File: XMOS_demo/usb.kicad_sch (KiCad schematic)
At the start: 15 parts, among them J2 Screw_Terminal, J3 Conn_01x02_Pin, J4 USB_C_Receptacle_USB2.0_16P, U3 TPD3S014

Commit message: Summary (required)
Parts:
- renumbered C22 to C30, C23 to C31, R16 to R21, R17 to R22, R24 to R23, R26 to R24, R18 to R25, R19 to R26
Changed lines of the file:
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@@
 		(on_board yes)
 		(dnp no)
-		(property "Reference" "#PWR094"
+		(property "Reference" "#PWR041"
 			(at 261.62 97.79 0)
 			(effects
@@
 			(project "XMOS_demo"
 				(path "/0a855fb0-ca19-4770-811e-70d8770d7fdd/0ad88a15-386f-4052-8899-c737373d7f63"
-					(reference "#PWR094")
+					(reference "#PWR041")
 					(unit 1)
 				)
@@
 		(on_board yes)
 		(dnp no)
-		(property "Reference" "R16"
+		(property "Reference" "R21"
 			(at 112.522 52.324 0)
 			(effects
@@
 			(project "XMOS_demo"
 				(path "/0a855fb0-ca19-4770-811e-70d8770d7fdd/0ad88a15-386f-4052-8899-c737373d7f63"
-					(reference "R16")
+					(reference "R21")
 					(unit 1)
 				)
@@
 		(on_board yes)
 		(dnp no)
-		(property "Reference" "R18"
+		(property "Reference" "R25"
 			(at 124.46 77.216 90)
 			(effects
@@
 			(project "XMOS_demo"
 				(path "/0a855fb0-ca19-4770-811e-70d8770d7fdd/0ad88a15-386f-4052-8899-c737373d7f63"
-					(reference "R18")
+					(reference "R25")
 					(unit 1)
 				)
@@
 		(on_board yes)
 		(dnp no)
-		(property "Reference" "#PWR036"
+		(property "Reference" "#PWR039"
 			(at 200.66 92.71 0)
 			(effects
@@
 			(project "XMOS_demo"
 				(path "/0a855fb0-ca19-4770-811e-70d8770d7fdd/0ad88a15-386f-4052-8899-c737373d7f63"
-					(reference "#PWR036")
+					(reference "#PWR039")
 					(unit 1)
 				)
@@
 		(on_board yes)
 		(dnp no)
-		(property "Reference" "#PWR027"
+		(property "Reference" "#PWR029"
 			(at 111.76 46.99 0)
 			(effects
@@
 			(project "XMOS_demo"
 				(path "/0a855fb0-ca19-4770-811e-70d8770d7fdd/0ad88a15-386f-4052-8899-c737373d7f63"
-					(reference "#PWR027")
+					(reference "#PWR029")
 					(unit 1)
 				)
@@
 		(on_board yes)
 		(dnp no)
-		(property "Reference" "#PWR054"
+		(property "Reference" "#PWR033"
 			(at 248.92 74.93 0)
 			(effects
@@
 			(project "XMOS_demo"
 				(path "/0a855fb0-ca19-4770-811e-70d8770d7fdd/0ad88a15-386f-4052-8899-c737373d7f63"
-					(reference "#PWR054")
+					(reference "#PWR033")
 					(unit 1)
 				)
@@
 		(on_board yes)
 		(dnp no)
-		(property "Reference" "#PWR029"
+		(property "Reference" "#PWR030"
 			(at 109.22 67.31 0)
 			(effects
@@
 			(project "XMOS_demo"
 				(path "/0a855fb0-ca19-4770-811e-70d8770d7fdd/0ad88a15-386f-4052-8899-c737373d7f63"
-					(reference "#PWR029")
+					(reference "#PWR030")
 					(unit 1)
 				)
@@
 		(on_board yes)
 		(dnp no)
-		(property "Reference" "#PWR095"
+		(property "Reference" "#PWR034"
 			(at 261.62 74.93 0)
 			(effects
@@
 			(project "XMOS_demo"
 				(path "/0a855fb0-ca19-4770-811e-70d8770d7fdd/0ad88a15-386f-4052-8899-c737373d7f63"
-					(reference "#PWR095")
+					(reference "#PWR034")
 					(unit 1)
 				)
@@
 		(on_board yes)
 		(dnp no)
-		(property "Reference" "R26"
+		(property "Reference" "R24"
 			(at 264.668 75.184 0)
 			(effects
@@
 			(project "XMOS_demo"
 				(path "/0a855fb0-ca19-4770-811e-70d8770d7fdd/0ad88a15-386f-4052-8899-c737373d7f63"
-					(reference "R26")
+					(reference "R24")
 					(unit 1)
 				)
@@
 		(on_board yes)
 		(dnp no)
-		(property "Reference" "C22"
+		(property "Reference" "C30"
 			(at 148.844 80.01 0)
 			(effects
@@
 			(project "XMOS_demo"
 				(path "/0a855fb0-ca19-4770-811e-70d8770d7fdd/0ad88a15-386f-4052-8899-c737373d7f63"
-					(reference "C22")
+					(reference "C30")
 					(unit 1)
 				)
@@
 		(on_board yes)
 		(dnp no)
-		(property "Reference" "C23"
+		(property "Reference" "C31"
 			(at 166.624 80.01 0)
 			(effects
@@
 			(project "XMOS_demo"
 				(path "/0a855fb0-ca19-4770-811e-70d8770d7fdd/0ad88a15-386f-4052-8899-c737373d7f63"
-					(reference "C23")
+					(reference "C31")
 					(unit 1)
 				)
@@
 		(on_board yes)
 		(dnp no)
-		(property "Reference" "#PWR030"
+		(property "Reference" "#PWR031"
 			(at 180.34 72.39 0)
 			(effects
@@
 			(project "XMOS_demo"
 				(path "/0a855fb0-ca19-4770-811e-70d8770d7fdd/0ad88a15-386f-4052-8899-c737373d7f63"
-					(reference "#PWR030")
+					(reference "#PWR031")
 					(unit 1)
 				)
@@
 		(on_board yes)
 		(dnp no)
-		(property "Reference" "#PWR031"
+		(property "Reference" "#PWR032"
 			(at 220.98 72.39 0)
 			(effects
@@
 			(project "XMOS_demo"
 				(path "/0a855fb0-ca19-4770-811e-70d8770d7fdd/0ad88a15-386f-4052-8899-c737373d7f63"
-					(reference "#PWR031")
+					(reference "#PWR032")
 					(unit 1)
 				)
@@
 		(dnp no)
 		(fields_autoplaced yes)
-		(property "Reference" "#FLG08"
+		(property "Reference" "#FLG05"
 			(at 86.36 112.395 0)
 			(effects
@@
 			(project "XMOS_demo"
 				(path "/0a855fb0-ca19-4770-811e-70d8770d7fdd/0ad88a15-386f-4052-8899-c737373d7f63"
-					(reference "#FLG08")
+					(reference "#FLG05")
 					(unit 1)
 				)
@@
 		(on_board yes)
 		(dnp no)
-		(property "Reference" "#PWR033"
+		(property "Reference" "#PWR036"
 			(at 137.16 92.71 0)
 			(effects
@@
 			(project "XMOS_demo"
 				(path "/0a855fb0-ca19-4770-811e-70d8770d7fdd/0ad88a15-386f-4052-8899-c737373d7f63"
-					(reference "#PWR033")
+					(reference "#PWR036")
 					(unit 1)
 				)
@@
 		(on_board yes)
 		(dnp no)
-		(property "Reference" "R24"
+		(property "Reference" "R23"
 			(at 251.968 75.184 0)
 			(effects
@@
 			(project "XMOS_demo"
 				(path "/0a855fb0-ca19-4770-811e-70d8770d7fdd/0ad88a15-386f-4052-8899-c737373d7f63"
-					(reference "R24")
+					(reference "R23")
 					(unit 1)
 				)
@@
 		(on_board yes)
 		(dnp no)
-		(property "Reference" "#PWR032"
+		(property "Reference" "#PWR035"
 			(at 139.7 77.47 0)
 			(effects
@@
 			(project "XMOS_demo"
 				(path "/0a855fb0-ca19-4770-811e-70d8770d7fdd/0ad88a15-386f-4052-8899-c737373d7f63"
-					(reference "#PWR032")
+					(reference "#PWR035")
 					(unit 1)
 				)
@@
 		(on_board yes)
 		(dnp no)
-		(property "Reference" "R17"
+		(property "Reference" "R22"
 			(at 185.42 74.676 90)
 			(effects
@@
 			(project "XMOS_demo"
 				(path "/0a855fb0-ca19-4770-811e-70d8770d7fdd/0ad88a15-386f-4052-8899-c737373d7f63"
-					(reference "R17")
+					(reference "R22")
 					(unit 1)
 				)
@@
 		(on_board yes)
 		(dnp no)
-		(property "Reference" "#PWR028"
+		(property "Reference" "#PWR040"
 			(at 248.92 97.79 0)
 			(effects
@@
 			(project "XMOS_demo"
 				(path "/0a855fb0-ca19-4770-811e-70d8770d7fdd/0ad88a15-386f-4052-8899-c737373d7f63"
-					(reference "#PWR028")
+					(reference "#PWR040")
 					(unit 1)
 				)
@@
 		(on_board yes)
 		(dnp no)
-		(property "Reference" "#PWR037"
+		(property "Reference" "#PWR042"
 			(at 104.14 125.73 0)
 			(effects
@@
 			(project "XMOS_demo"
 				(path "/0a855fb0-ca19-4770-811e-70d8770d7fdd/0ad88a15-386f-4052-8899-c737373d7f63"
-					(reference "#PWR037")
+					(reference "#PWR042")
 					(unit 1)
 				)
@@
 		(on_board yes)
 		(dnp no)
-		(property "Reference" "R19"
+		(property "Reference" "R26"
 			(at 129.54 85.852 90)
 			(effects
@@
 			(project "XMOS_demo"
 				(path "/0a855fb0-ca19-4770-811e-70d8770d7fdd/0ad88a15-386f-4052-8899-c737373d7f63"
-					(reference "R19")
+					(reference "R26")
 					(unit 1)
 				)
@@
 		(on_board yes)
 		(dnp no)
-		(property "Reference" "#PWR035"
+		(property "Reference" "#PWR038"
 			(at 165.1 92.71 0)
 			(effects
@@
 			(project "XMOS_demo"
 				(path "/0a855fb0-ca19-4770-811e-70d8770d7fdd/0ad88a15-386f-4052-8899-c737373d7f63"
-					(reference "#PWR035")
+					(reference "#PWR038")
 					(unit 1)
 				)
@@
 		(on_board yes)
 		(dnp no)
-		(property "Reference" "#PWR034"
+		(property "Reference" "#PWR037"
 			(at 147.32 92.71 0)
 			(effects
@@
 			(project "XMOS_demo"
 				(path "/0a855fb0-ca19-4770-811e-70d8770d7fdd/0ad88a15-386f-4052-8899-c737373d7f63"
-					(reference "#PWR034")
-					(unit 1)
-				)
+					(reference "#PWR037")
+					(unit 1)
+				)

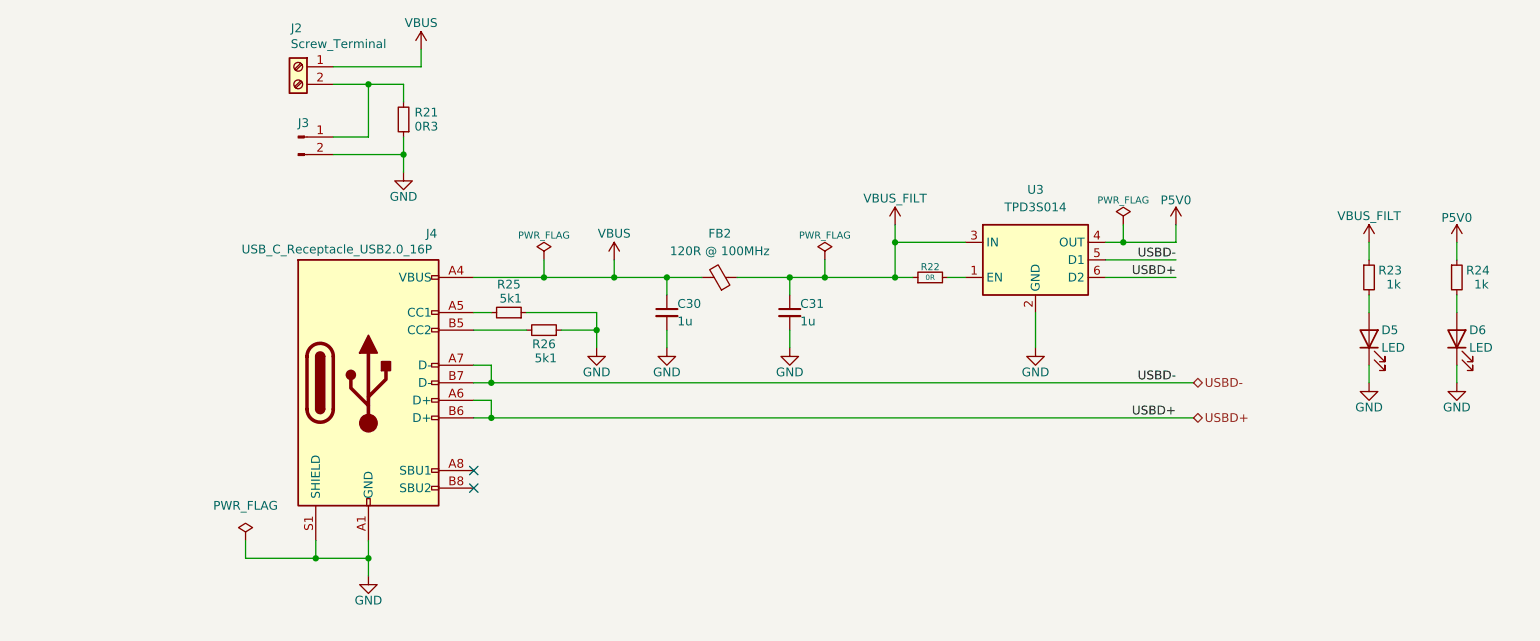
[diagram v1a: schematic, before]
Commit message: Started changes on power supply (audio in) on schematic
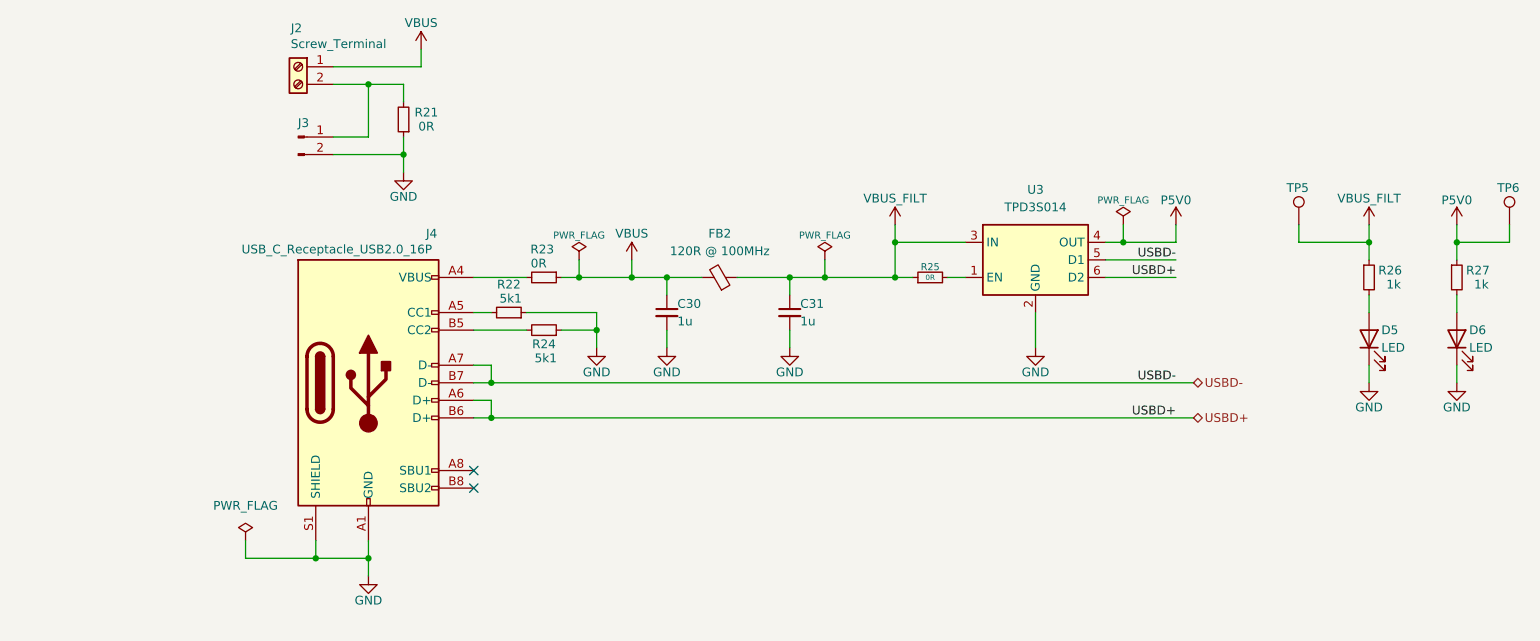
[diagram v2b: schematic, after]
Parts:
- added R23: 0R, Resistor_SMD:R_0603_1608Metric, symbol Device:R_Small
- added TP5, TP6: TestPoint, TestPoint:TestPoint_Keystone_5005-5009_Compact, symbol Connector:TestPoint
- R21: value 0R3 -> 0R
- renumbered R25 to R22, R26 to R24, R22 to R25, R23 to R26, R24 to R27
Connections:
- net P5V0: now also TP6.1
- net VBUS: now also R23.1; no longer J4.A4 (VBUS), J4.A9 (VBUS), J4.B4 (VBUS), J4.B9 (VBUS)
- net VBUS_FILT: now also TP5.1
- new net: J4.A4 (VBUS), J4.A9 (VBUS), J4.B4 (VBUS), J4.B9 (VBUS), R23.2

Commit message: Passive lpf added to autio output
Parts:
- renumbered R21 to R16, R23 to R17, R25 to R18, R26 to R19, R27 to R20, R22 to R21, R24 to R22
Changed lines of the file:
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@@
 		(on_board yes)
 		(dnp no)
-		(property "Reference" "#PWR042"
+		(property "Reference" "#PWR041"
 			(at 261.62 97.79 0)
 			(effects
@@
 			(project "XMOS_demo"
 				(path "/0a855fb0-ca19-4770-811e-70d8770d7fdd/0ad88a15-386f-4052-8899-c737373d7f63"
-					(reference "#PWR042")
+					(reference "#PWR041")
 					(unit 1)
 				)
@@
 		(on_board yes)
 		(dnp no)
-		(property "Reference" "R21"
+		(property "Reference" "R16"
 			(at 112.522 52.324 0)
 			(effects
@@
 			(project "XMOS_demo"
 				(path "/0a855fb0-ca19-4770-811e-70d8770d7fdd/0ad88a15-386f-4052-8899-c737373d7f63"
-					(reference "R21")
+					(reference "R16")
 					(unit 1)
 				)
@@
 		(on_board yes)
 		(dnp no)
-		(property "Reference" "R22"
+		(property "Reference" "R21"
 			(at 124.46 77.216 90)
 			(effects
@@
 			(project "XMOS_demo"
 				(path "/0a855fb0-ca19-4770-811e-70d8770d7fdd/0ad88a15-386f-4052-8899-c737373d7f63"
-					(reference "R22")
+					(reference "R21")
 					(unit 1)
 				)
@@
 		(on_board yes)
 		(dnp no)
-		(property "Reference" "#PWR037"
+		(property "Reference" "#PWR039"
 			(at 200.66 92.71 0)
 			(effects
@@
 			(project "XMOS_demo"
 				(path "/0a855fb0-ca19-4770-811e-70d8770d7fdd/0ad88a15-386f-4052-8899-c737373d7f63"
-					(reference "#PWR037")
+					(reference "#PWR039")
 					(unit 1)
 				)
@@
 		(on_board yes)
 		(dnp no)
-		(property "Reference" "#PWR031"
+		(property "Reference" "#PWR029"
 			(at 111.76 46.99 0)
 			(effects
@@
 			(project "XMOS_demo"
 				(path "/0a855fb0-ca19-4770-811e-70d8770d7fdd/0ad88a15-386f-4052-8899-c737373d7f63"
-					(reference "#PWR031")
+					(reference "#PWR029")
 					(unit 1)
 				)
@@
 		(on_board yes)
 		(dnp no)
-		(property "Reference" "#FLG05"
+		(property "Reference" "#FLG02"
 			(at 213.36 66.675 0)
 			(effects
@@
 			(project "XMOS_demo"
 				(path "/0a855fb0-ca19-4770-811e-70d8770d7fdd/0ad88a15-386f-4052-8899-c737373d7f63"
-					(reference "#FLG05")
+					(reference "#FLG02")
 					(unit 1)
 				)
@@
 		(on_board yes)
 		(dnp no)
-		(property "Reference" "#PWR039"
+		(property "Reference" "#PWR033"
 			(at 248.92 72.39 0)
 			(effects
@@
 			(project "XMOS_demo"
 				(path "/0a855fb0-ca19-4770-811e-70d8770d7fdd/0ad88a15-386f-4052-8899-c737373d7f63"
-					(reference "#PWR039")
+					(reference "#PWR033")
 					(unit 1)
 				)
@@
 		(on_board yes)
 		(dnp no)
-		(property "Reference" "#PWR041"
+		(property "Reference" "#PWR034"
 			(at 261.62 72.39 0)
 			(effects
@@
 			(project "XMOS_demo"
 				(path "/0a855fb0-ca19-4770-811e-70d8770d7fdd/0ad88a15-386f-4052-8899-c737373d7f63"
-					(reference "#PWR041")
+					(reference "#PWR034")
 					(unit 1)
 				)
@@
 		(on_board yes)
 		(dnp no)
-		(property "Reference" "R27"
+		(property "Reference" "R20"
 			(at 264.668 75.184 0)
 			(effects
@@
 			(project "XMOS_demo"
 				(path "/0a855fb0-ca19-4770-811e-70d8770d7fdd/0ad88a15-386f-4052-8899-c737373d7f63"
-					(reference "R27")
+					(reference "R20")
 					(unit 1)
 				)
@@
 		(on_board yes)
 		(dnp no)
-		(property "Reference" "#PWR036"
+		(property "Reference" "#PWR031"
 			(at 180.34 72.39 0)
 			(effects
@@
 			(project "XMOS_demo"
 				(path "/0a855fb0-ca19-4770-811e-70d8770d7fdd/0ad88a15-386f-4052-8899-c737373d7f63"
-					(reference "#PWR036")
+					(reference "#PWR031")
 					(unit 1)
 				)
@@
 		(on_board yes)
 		(dnp no)
-		(property "Reference" "#PWR038"
+		(property "Reference" "#PWR032"
 			(at 220.98 72.39 0)
 			(effects
@@
 			(project "XMOS_demo"
 				(path "/0a855fb0-ca19-4770-811e-70d8770d7fdd/0ad88a15-386f-4052-8899-c737373d7f63"
-					(reference "#PWR038")
+					(reference "#PWR032")
 					(unit 1)
 				)
@@
 		(dnp no)
 		(fields_autoplaced yes)
-		(property "Reference" "#FLG02"
+		(property "Reference" "#FLG05"
 			(at 86.36 112.395 0)
 			(effects
@@
 			(project "XMOS_demo"
 				(path "/0a855fb0-ca19-4770-811e-70d8770d7fdd/0ad88a15-386f-4052-8899-c737373d7f63"
-					(reference "#FLG02")
+					(reference "#FLG05")
 					(unit 1)
 				)
@@
 		(on_board yes)
 		(dnp no)
-		(property "Reference" "#PWR032"
+		(property "Reference" "#PWR036"
 			(at 137.16 92.71 0)
 			(effects
@@
 			(project "XMOS_demo"
 				(path "/0a855fb0-ca19-4770-811e-70d8770d7fdd/0ad88a15-386f-4052-8899-c737373d7f63"
-					(reference "#PWR032")
+					(reference "#PWR036")
 					(unit 1)
 				)
@@
 		(on_board yes)
 		(dnp no)
-		(property "Reference" "R26"
+		(property "Reference" "R19"
 			(at 251.968 75.184 0)
 			(effects
@@
 			(project "XMOS_demo"
 				(path "/0a855fb0-ca19-4770-811e-70d8770d7fdd/0ad88a15-386f-4052-8899-c737373d7f63"
-					(reference "R26")
+					(reference "R19")
 					(unit 1)
 				)
@@
 		(on_board yes)
 		(dnp no)
-		(property "Reference" "#PWR033"
+		(property "Reference" "#PWR035"
 			(at 142.24 77.47 0)
 			(effects
@@
 			(project "XMOS_demo"
 				(path "/0a855fb0-ca19-4770-811e-70d8770d7fdd/0ad88a15-386f-4052-8899-c737373d7f63"
-					(reference "#PWR033")
+					(reference "#PWR035")
 					(unit 1)
 				)
@@
 		(on_board yes)
 		(dnp no)
-		(property "Reference" "R25"
+		(property "Reference" "R18"
 			(at 185.42 74.676 90)
 			(effects
@@
 			(project "XMOS_demo"
 				(path "/0a855fb0-ca19-4770-811e-70d8770d7fdd/0ad88a15-386f-4052-8899-c737373d7f63"
-					(reference "R25")
+					(reference "R18")
 					(unit 1)
 				)
@@
 		(on_board yes)
 		(dnp no)
-		(property "Reference" "#PWR029"
+		(property "Reference" "#PWR042"
 			(at 104.14 125.73 0)
 			(effects
@@
 			(project "XMOS_demo"
 				(path "/0a855fb0-ca19-4770-811e-70d8770d7fdd/0ad88a15-386f-4052-8899-c737373d7f63"
-					(reference "#PWR029")
+					(reference "#PWR042")
 					(unit 1)
 				)
@@
 		(on_board yes)
 		(dnp no)
-		(property "Reference" "R23"
+		(property "Reference" "R17"
 			(at 129.286 72.136 90)
 			(effects
@@
 			(project "XMOS_demo"
 				(path "/0a855fb0-ca19-4770-811e-70d8770d7fdd/0ad88a15-386f-4052-8899-c737373d7f63"
-					(reference "R23")
+					(reference "R17")
 					(unit 1)
 				)
@@
 		(on_board yes)
 		(dnp no)
-		(property "Reference" "R24"
+		(property "Reference" "R22"
 			(at 129.54 85.852 90)
 			(effects
@@
 			(project "XMOS_demo"
 				(path "/0a855fb0-ca19-4770-811e-70d8770d7fdd/0ad88a15-386f-4052-8899-c737373d7f63"
-					(reference "R24")
+					(reference "R22")
 					(unit 1)
 				)
@@
 		(on_board yes)
 		(dnp no)
-		(property "Reference" "#PWR035"
+		(property "Reference" "#PWR038"
 			(at 165.1 92.71 0)
 			(effects
@@
 			(project "XMOS_demo"
 				(path "/0a855fb0-ca19-4770-811e-70d8770d7fdd/0ad88a15-386f-4052-8899-c737373d7f63"
-					(reference "#PWR035")
+					(reference "#PWR038")
 					(unit 1)
 				)
@@
 		(on_board yes)
 		(dnp no)
-		(property "Reference" "#PWR034"
+		(property "Reference" "#PWR037"
 			(at 147.32 92.71 0)
 			(effects
@@
 			(project "XMOS_demo"
 				(path "/0a855fb0-ca19-4770-811e-70d8770d7fdd/0ad88a15-386f-4052-8899-c737373d7f63"
-					(reference "#PWR034")
-					(unit 1)
-				)
+					(reference "#PWR037")
+					(unit 1)
+				)

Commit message: PCB work
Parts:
- added C30, C31: 100u, Capacitor_SMD:CP_Elec_6.3x5.7, symbol Device:C_Polarized_Small
- renumbered C30 to C32, C31 to C33
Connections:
- net GND: now also C30.2, C31.2
- net P5V0: now also C30.1, C31.1
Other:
- moved on the sheet: C32, C33, D5, D6, FB2, J2, J3, J4, R16, R17, R18, R19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
